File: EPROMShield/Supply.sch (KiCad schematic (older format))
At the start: 21 parts

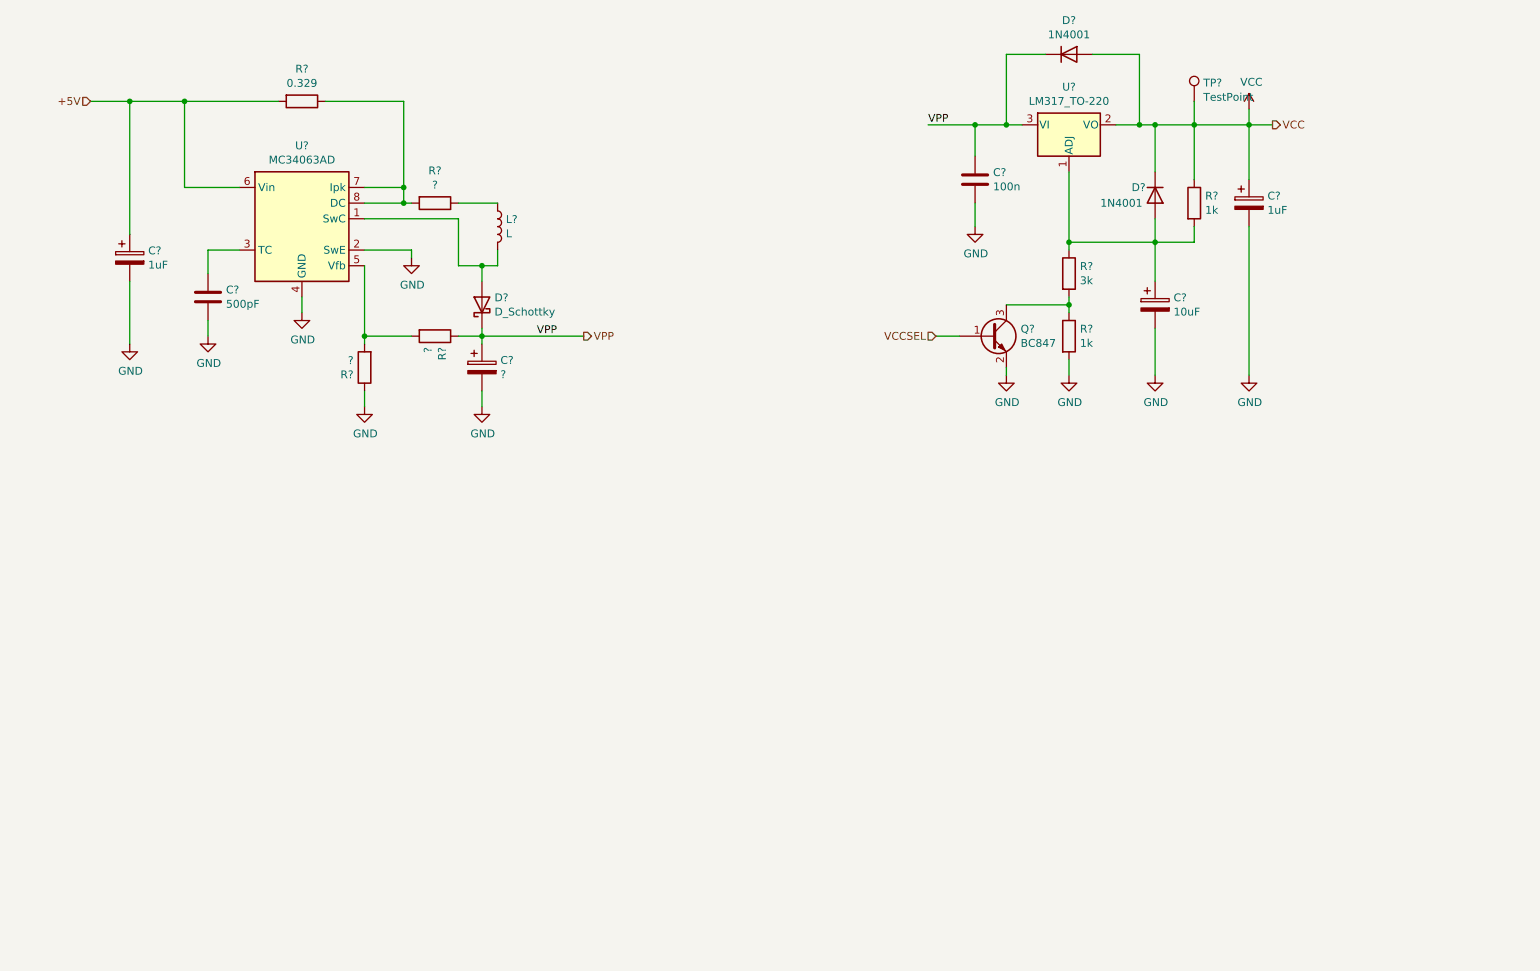
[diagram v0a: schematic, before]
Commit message: Finished schematic added caluclation for boost converter
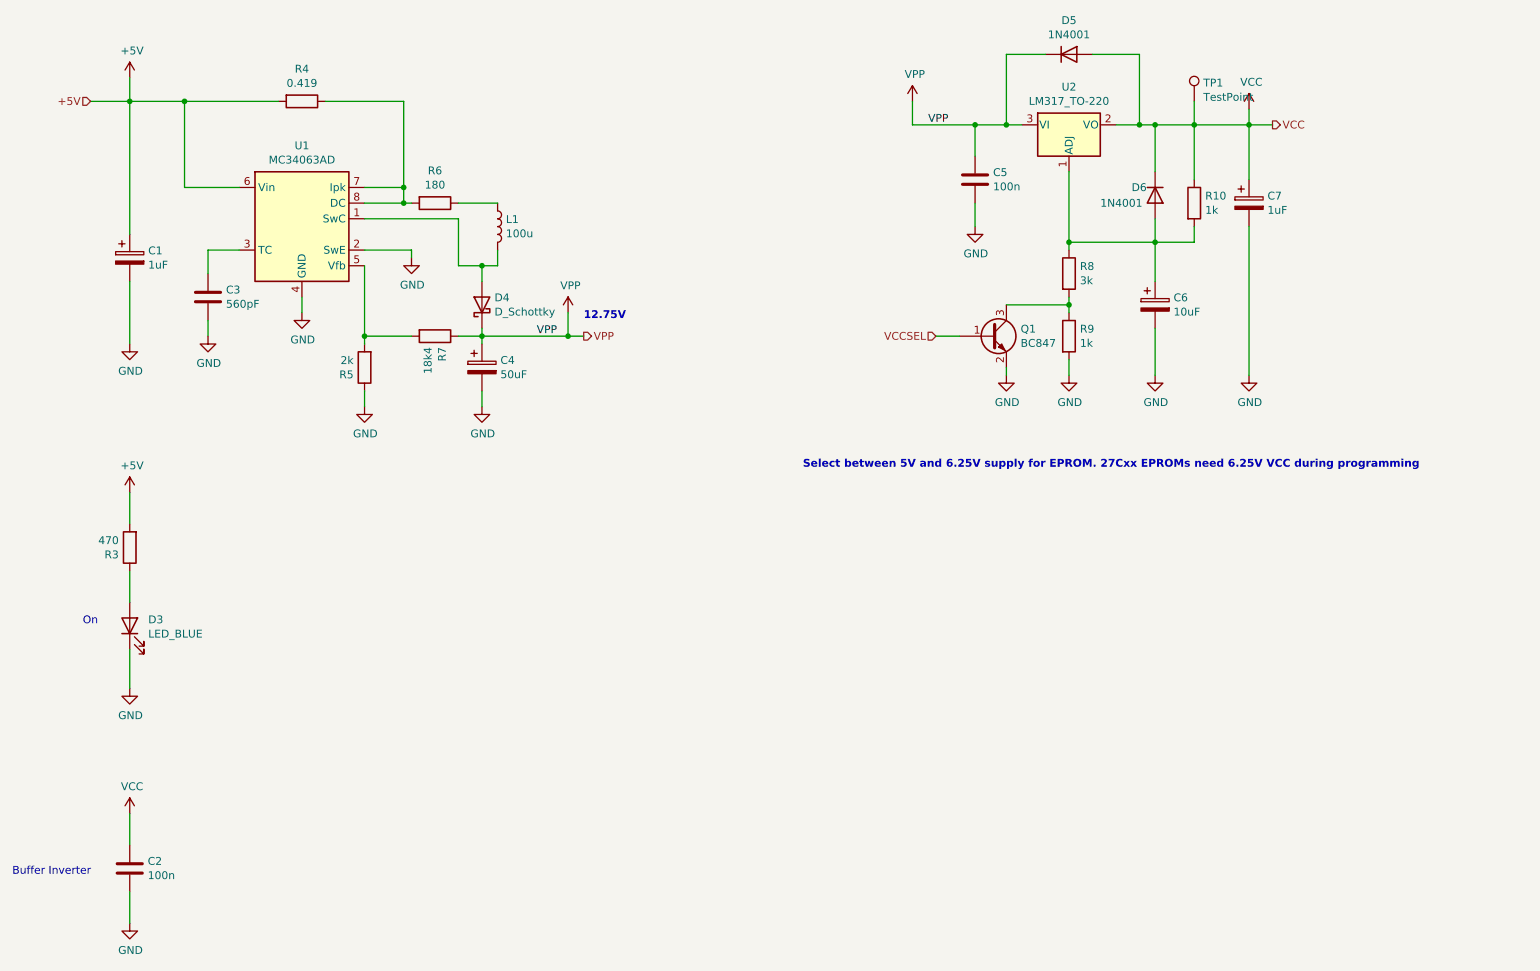
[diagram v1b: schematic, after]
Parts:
- added C2: 100n, symbol Device:C
- added D3: LED_BLUE, symbol Device:LED
- added R3: 470, symbol Device:R
- C3: renamed from C?; value 500pF -> 560pF
- C4: renamed from C?; value ? -> 50uF
- L1: renamed from L?; value L -> 100u
- R4: renamed from R?; value 0.329 -> 0.419
- R5: renamed from R?; value ? -> 2k
- R6: renamed from R?; value ? -> 180
- R7: renamed from R?; value ? -> 18k4
- gave numbers to parts that had none: 14
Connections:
- net +5V: now also R3.2
- net GND: now also C2.2, D3.1 (K)
- net VCC: now also C2.1
- new net: D3.2 (A), R3.1
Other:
- note added: "12.75V"
- note added: "Buffer Inverter"
- note added: "On"
- note added: "Select between 5V and 6.25V supply for EPROM. 27Cxx EPROMs need 6.25V VCC during programming"

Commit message: Footprints associated
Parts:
- C1: footprint (none) -> Capacitor_THT:CP_Radial_D4.0mm_P1.50mm
- C2, C3, C5: footprint (none) -> Capacitor_SMD:C_0805_2012Metric_Pad1.18x1.45mm_HandSolder
- C4, C6, L1: footprint (none) -> Capacitor_THT:CP_Radial_D6.3mm_P2.50mm
- C7: footprint (none) -> Capacitor_THT:CP_Radial_D5.0mm_P2.50mm
- D3: footprint (none) -> LED_SMD:LED_1206_3216Metric_Pad1.42x1.75mm_HandSolder
- D4: value D_Schottky -> SK26ASMD; footprint (none) -> Diode_SMD:D_SMA_Handsoldering
- R10, R3, R5, R6, R7, R8, R9: footprint (none) -> Resistor_SMD:R_0805_2012Metric_Pad1.20x1.40mm_HandSolder
- R4: value 0.419 -> 0.3; footprint (none) -> Resistor_SMD:R_1206_3216Metric_Pad1.30x1.75mm_HandSolder
- TP1: footprint (none) -> TestPoint:TestPoint_Pad_D2.0mm
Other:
- moved on the sheet: C2
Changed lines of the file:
@@
 F 0 "C3" H 2365 2696 50  0000 L CNN
 F 1 "560pF" H 2365 2605 50  0000 L CNN
-F 2 "" H 2288 2500 50  0001 C CNN
+F 2 "Capacitor_SMD:C_0805_2012Metric_Pad1.18x1.45mm_HandSolder" H 2288 2500 50  0001 C CNN
 F 3 "~" H 2250 2650 50  0001 C CNN
 	1    2250 2650
@@
 F 0 "R10" H 8620 2096 50  0000 L CNN
 F 1 "1k" H 8620 2005 50  0000 L CNN
-F 2 "" V 8480 2050 50  0001 C CNN
+F 2 "Resistor_SMD:R_0805_2012Metric_Pad1.20x1.40mm_HandSolder" V 8480 2050 50  0001 C CNN
 F 3 "~" H 8550 2050 50  0001 C CNN
 	1    8550 2050
@@
 F 0 "R8" H 7820 2546 50  0000 L CNN
 F 1 "3k" H 7820 2455 50  0000 L CNN
-F 2 "" V 7680 2500 50  0001 C CNN
+F 2 "Resistor_SMD:R_0805_2012Metric_Pad1.20x1.40mm_HandSolder" V 7680 2500 50  0001 C CNN
 F 3 "~" H 7750 2500 50  0001 C CNN
 	1    7750 2500
@@
 F 0 "R9" H 7820 2946 50  0000 L CNN
 F 1 "1k" H 7820 2855 50  0000 L CNN
-F 2 "" V 7680 2900 50  0001 C CNN
+F 2 "Resistor_SMD:R_0805_2012Metric_Pad1.20x1.40mm_HandSolder" V 7680 2900 50  0001 C CNN
 F 3 "~" H 7750 2900 50  0001 C CNN
 	1    7750 2900
@@
 F 0 "C6" H 8418 2746 50  0000 L CNN
 F 1 "10uF" H 8418 2655 50  0000 L CNN
-F 2 "" H 8338 2550 50  0001 C CNN
+F 2 "Capacitor_THT:CP_Radial_D6.3mm_P2.50mm" H 8338 2550 50  0001 C CNN
 F 3 "~" H 8300 2700 50  0001 C CNN
 	1    8300 2700
@@
 F 0 "C7" H 9018 2096 50  0000 L CNN
 F 1 "1uF" H 9018 2005 50  0000 L CNN
-F 2 "" H 8938 1900 50  0001 C CNN
+F 2 "Capacitor_THT:CP_Radial_D5.0mm_P2.50mm" H 8938 1900 50  0001 C CNN
 F 3 "~" H 8900 2050 50  0001 C CNN
 	1    8900 2050
@@
 F 0 "C5" H 7265 1946 50  0000 L CNN
 F 1 "100n" H 7265 1855 50  0000 L CNN
-F 2 "" H 7188 1750 50  0001 C CNN
+F 2 "Capacitor_SMD:C_0805_2012Metric_Pad1.18x1.45mm_HandSolder" H 7188 1750 50  0001 C CNN
 F 3 "~" H 7150 1900 50  0001 C CNN
 	1    7150 1900
@@
 F 0 "TP1" H 8608 1518 50  0000 L CNN
 F 1 "TestPoint" H 8608 1427 50  0000 L CNN
-F 2 "" H 8750 1400 50  0001 C CNN
+F 2 "TestPoint:TestPoint_Pad_D2.0mm" H 8750 1400 50  0001 C CNN
 F 3 "~" H 8750 1400 50  0001 C CNN
 	1    8550 1400
@@
 P 2850 1400
 F 0 "R4" V 2643 1400 50  0000 C CNN
-F 1 "0.419" V 2734 1400 50  0000 C CNN
-F 2 "" V 2780 1400 50  0001 C CNN
+F 1 "0.3" V 2734 1400 50  0000 C CNN
+F 2 "Resistor_SMD:R_1206_3216Metric_Pad1.30x1.75mm_HandSolder" V 2780 1400 50  0001 C CNN
 F 3 "~" H 2850 1400 50  0001 C CNN
 	1    2850 1400
@@
 F 0 "R6" V 3493 2050 50  0000 C CNN
 F 1 "180" V 3584 2050 50  0000 C CNN
-F 2 "" V 3630 2050 50  0001 C CNN
+F 2 "Resistor_SMD:R_0805_2012Metric_Pad1.20x1.40mm_HandSolder" V 3630 2050 50  0001 C CNN
 F 3 "~" H 3700 2050 50  0001 C CNN
 	1    3700 2050
@@
 F 0 "L1" H 4153 2246 50  0000 L CNN
 F 1 "100u" H 4153 2155 50  0000 L CNN
-F 2 "" H 4100 2200 50  0001 C CNN
+F 2 "Capacitor_THT:CP_Radial_D6.3mm_P2.50mm" H 4100 2200 50  0001 C CNN
 F 3 "~" H 4100 2200 50  0001 C CNN
 	1    4100 2200
@@
 P 4000 2700
 F 0 "D4" V 4046 2620 50  0000 R CNN
-F 1 "D_Schottky" V 3955 2620 50  0000 R CNN
-F 2 "" H 4000 2700 50  0001 C CNN
+F 1 "SK26ASMD" V 3955 2620 50  0000 R CNN
+F 2 "Diode_SMD:D_SMA_Handsoldering" H 4000 2700 50  0001 C CNN
 F 3 "~" H 4000 2700 50  0001 C CNN
 	1    4000 2700
@@
 F 0 "C4" H 4118 3146 50  0000 L CNN
 F 1 "50uF" H 4118 3055 50  0000 L CNN
-F 2 "" H 4038 2950 50  0001 C CNN
+F 2 "Capacitor_THT:CP_Radial_D6.3mm_P2.50mm" H 4038 2950 50  0001 C CNN
 F 3 "~" H 4000 3100 50  0001 C CNN
 	1    4000 3100
@@
 F 0 "R7" H 3770 2946 50  0000 L CNN
 F 1 "18k4" H 3770 2855 50  0000 L CNN
-F 2 "" V 3630 2900 50  0001 C CNN
+F 2 "Resistor_SMD:R_0805_2012Metric_Pad1.20x1.40mm_HandSolder" V 3630 2900 50  0001 C CNN
 F 3 "~" H 3700 2900 50  0001 C CNN
 	1    3700 2900
@@
 F 0 "R5" H 3320 3146 50  0000 L CNN
 F 1 "2k" H 3320 3055 50  0000 L CNN
-F 2 "" V 3180 3100 50  0001 C CNN
+F 2 "Resistor_SMD:R_0805_2012Metric_Pad1.20x1.40mm_HandSolder" V 3180 3100 50  0001 C CNN
 F 3 "~" H 3250 3100 50  0001 C CNN
 	1    3250 3100
@@
 F 0 "C1" H 1868 2446 50  0000 L CNN
 F 1 "1uF" H 1868 2355 50  0000 L CNN
-F 2 "" H 1788 2250 50  0001 C CNN
+F 2 "Capacitor_THT:CP_Radial_D4.0mm_P1.50mm" H 1788 2250 50  0001 C CNN
 F 3 "~" H 1750 2400 50  0001 C CNN
 	1    1750 2400
@@
 F 0 "D3" V 1789 4632 50  0000 R CNN
 F 1 "LED_BLUE" V 1698 4632 50  0000 R CNN
-F 2 "" H 1750 4750 50  0001 C CNN
+F 2 "LED_SMD:LED_1206_3216Metric_Pad1.42x1.75mm_HandSolder" H 1750 4750 50  0001 C CNN
 F 3 "~" H 1750 4750 50  0001 C CNN
 	1    1750 4750
@@
 F 0 "R3" H 1820 4296 50  0000 L CNN
 F 1 "470" H 1820 4205 50  0000 L CNN
-F 2 "" V 1680 4250 50  0001 C CNN
+F 2 "Resistor_SMD:R_0805_2012Metric_Pad1.20x1.40mm_HandSolder" V 1680 4250 50  0001 C CNN
 F 3 "~" H 1750 4250 50  0001 C CNN
 	1    1750 4250
@@
 L power:VCC #PWR0124
 U 1 1 61422861
-P 1750 5950
-F 0 "#PWR0124" H 1750 5800 50  0001 C CNN
-F 1 "VCC" H 1765 6123 50  0000 C CNN
-F 2 "" H 1750 5950 50  0001 C CNN
-F 3 "" H 1750 5950 50  0001 C CNN
-	1    1750 5950
+P 1750 5900
+F 0 "#PWR0124" H 1750 5750 50  0001 C CNN
+F 1 "VCC" H 1765 6073 50  0000 C CNN
+F 2 "" H 1750 5900 50  0001 C CNN
+F 3 "" H 1750 5900 50  0001 C CNN
+	1    1750 5900
 	1    0    0    -1
 $EndComp
@@
 L Device:C C2
 U 1 1 61423766
-P 1750 6300
-F 0 "C2" H 1865 6346 50  0000 L CNN
-F 1 "100n" H 1865 6255 50  0000 L CNN
-F 2 "" H 1788 6150 50  0001 C CNN
-F 3 "~" H 1750 6300 50  0001 C CNN
-	1    1750 6300
+P 1750 6250
+F 0 "C2" H 1865 6296 50  0000 L CNN
+F 1 "100n" H 1865 6205 50  0000 L CNN
+F 2 "Capacitor_SMD:C_0805_2012Metric_Pad1.18x1.45mm_HandSolder" H 1788 6100 50  0001 C CNN
+F 3 "~" H 1750 6250 50  0001 C CNN
+	1    1750 6250
 	1    0    0    -1
 $EndComp
@@
 L power:GND #PWR?
 U 1 1 61424590
-P 1750 6650
+P 1750 6600
 AR Path="/61424590" Ref="#PWR?"  Part="1"
 AR Path="/6162FE01/61424590" Ref="#PWR0125"  Part="1"
-F 0 "#PWR0125" H 1750 6400 50  0001 C CNN
-F 1 "GND" H 1755 6477 50  0000 C CNN
-F 2 "" H 1750 6650 50  0001 C CNN
-F 3 "" H 1750 6650 50  0001 C CNN
-	1    1750 6650
-	1    0    0    -1
-$EndComp
-Wire Wire Line
-	1750 5950 1750 6150
-Wire Wire Line
-	1750 6450 1750 6650
-Text Notes 1000 6350 0    50   ~ 0
+F 0 "#PWR0125" H 1750 6350 50  0001 C CNN
+F 1 "GND" H 1755 6427 50  0000 C CNN
+F 2 "" H 1750 6600 50  0001 C CNN
+F 3 "" H 1750 6600 50  0001 C CNN
+	1    1750 6600
+	1    0    0    -1
+$EndComp
+Wire Wire Line
+	1750 5900 1750 6100
+Wire Wire Line
+	1750 6400 1750 6600
+Text Notes 1000 6300 0    50   ~ 0
 Buffer Inverter
 $Comp

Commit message: Added netlist, fixed footprint L1
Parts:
- L1: footprint Capacitor_THT:CP_Radial_D6.3mm_P2.50mm -> Inductor_SMD:L_Fastron_PISN_Handsoldering
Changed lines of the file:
@@
 F 0 "L1" H 4153 2246 50  0000 L CNN
 F 1 "100u" H 4153 2155 50  0000 L CNN
-F 2 "Capacitor_THT:CP_Radial_D6.3mm_P2.50mm" H 4100 2200 50  0001 C CNN
+F 2 "Inductor_SMD:L_Fastron_PISN_Handsoldering" H 4100 2200 50  0001 C CNN
 F 3 "~" H 4100 2200 50  0001 C CNN
 	1    4100 2200

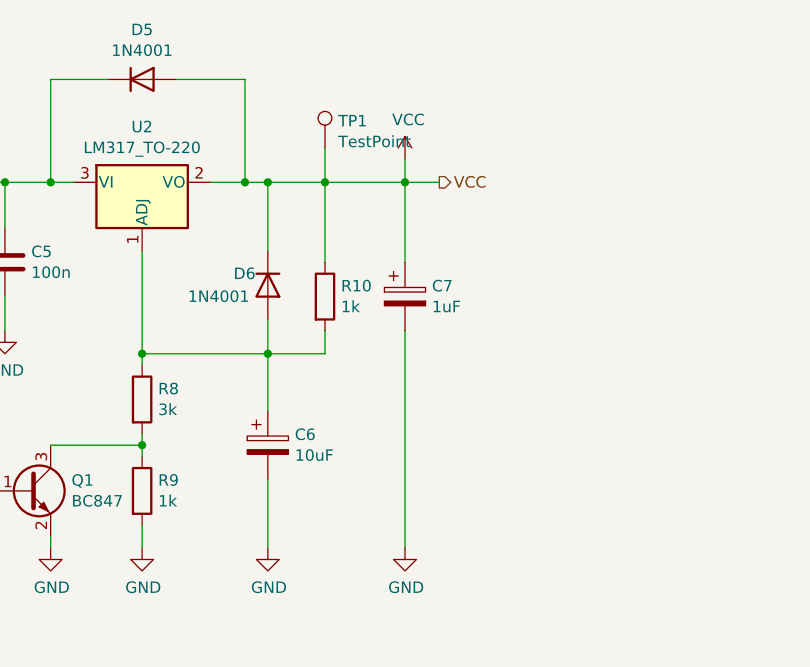
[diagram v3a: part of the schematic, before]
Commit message: First shot at component placement. Fixed VCC connection for Inverter
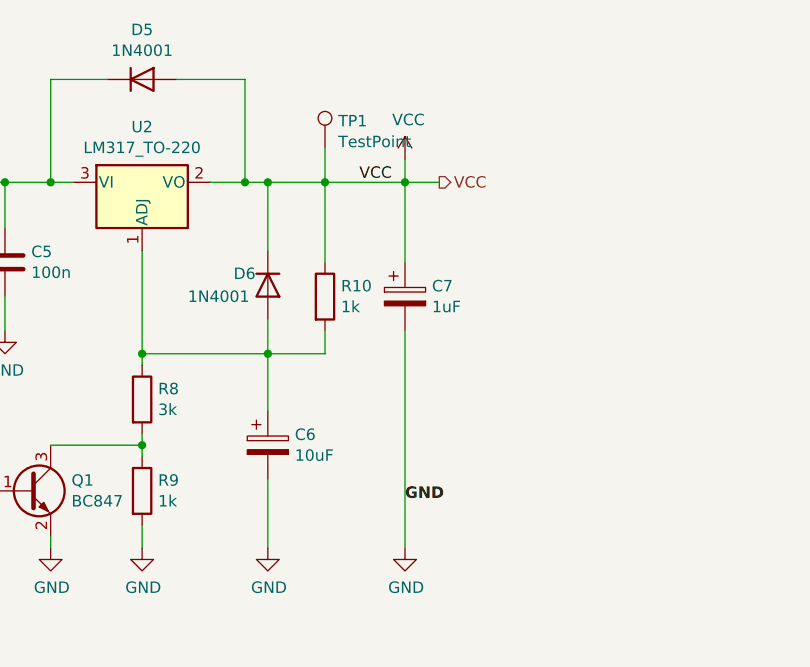
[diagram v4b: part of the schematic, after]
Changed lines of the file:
@@
 $EndComp
-Wire Wire Line
-	3250 2350 3550 2350
 Wire Wire Line
 	3550 2350 3550 2400
@@
 $EndComp
 Wire Wire Line
-	1750 5900 1750 6100
-Wire Wire Line
 	1750 6400 1750 6600
 Text Notes 1000 6300 0    50   ~ 0
@@
 Text Notes 4650 2800 0    50   ~ 10
 12.75V
+Wire Wire Line
+	1750 5900 1750 6100
+Text Label 8700 1550 0    50   ~ 0
+VCC
+Text Label 8900 2950 0    50   ~ 10
+GND
+Wire Wire Line
+	3250 2350 3550 2350
 $EndSCHEMATC

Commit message: First Version routing is done
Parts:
- D5, D6: footprint Diode_THT:D_DO-41_SOD81_P10.16mm_Horizontal -> Diode_SMD:D_MELF
- U2: footprint Package_TO_SOT_THT:TO-220-3_Vertical -> Package_TO_SOT_THT:TO-220F-3_Horizontal_TabDown
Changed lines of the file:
@@
 F 0 "U2" H 7750 1792 50  0000 C CNN
 F 1 "LM317_TO-220" H 7750 1701 50  0000 C CNN
-F 2 "Package_TO_SOT_THT:TO-220-3_Vertical" H 7750 1800 50  0001 C CIN
+F 2 "Package_TO_SOT_THT:TO-220F-3_Horizontal_TabDown" H 7750 1800 50  0001 C CIN
 F 3 "http://www.ti.com/lit/ds/symlink/lm317.pdf" H 7750 1550 50  0001 C CNN
 	1    7750 1550
@@
 F 0 "D6" V 8250 1850 50  0000 L CNN
 F 1 "1N4001" V 8350 1650 50  0000 L CNN
-F 2 "Diode_THT:D_DO-41_SOD81_P10.16mm_Horizontal" H 8300 1825 50  0001 C CNN
+F 2 "Diode_SMD:D_MELF" H 8300 1825 50  0001 C CNN
 F 3 "http://www.vishay.com/docs/88503/1n4001.pdf" H 8300 2000 50  0001 C CNN
 	1    8300 2000
@@
 F 0 "D5" H 7750 1317 50  0000 C CNN
 F 1 "1N4001" H 7750 1226 50  0000 C CNN
-F 2 "Diode_THT:D_DO-41_SOD81_P10.16mm_Horizontal" H 7750 925 50  0001 C CNN
+F 2 "Diode_SMD:D_MELF" H 7750 925 50  0001 C CNN
 F 3 "http://www.vishay.com/docs/88503/1n4001.pdf" H 7750 1100 50  0001 C CNN
 	1    7750 1100
